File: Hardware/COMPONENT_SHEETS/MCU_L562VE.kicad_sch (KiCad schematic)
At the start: 29 parts, among them SW1 MCU Reset, U7 STM32L562VET6Q, Y3 32MHz

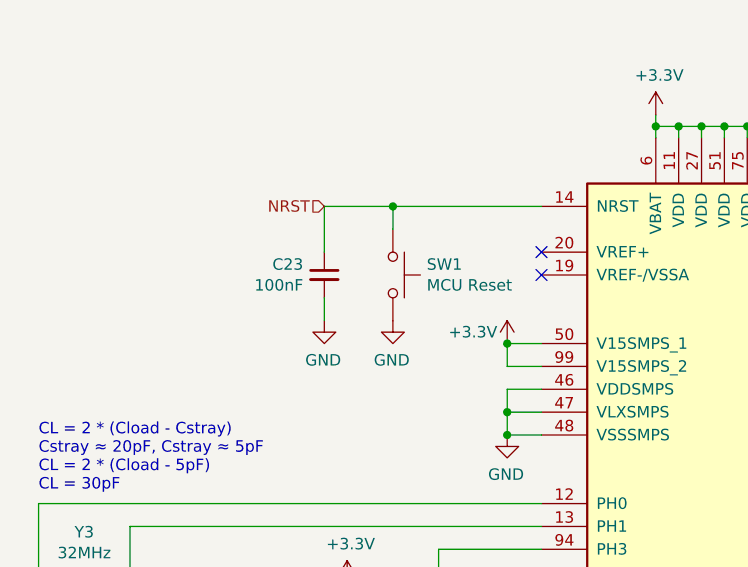
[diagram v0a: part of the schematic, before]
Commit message: Grounded VSSA
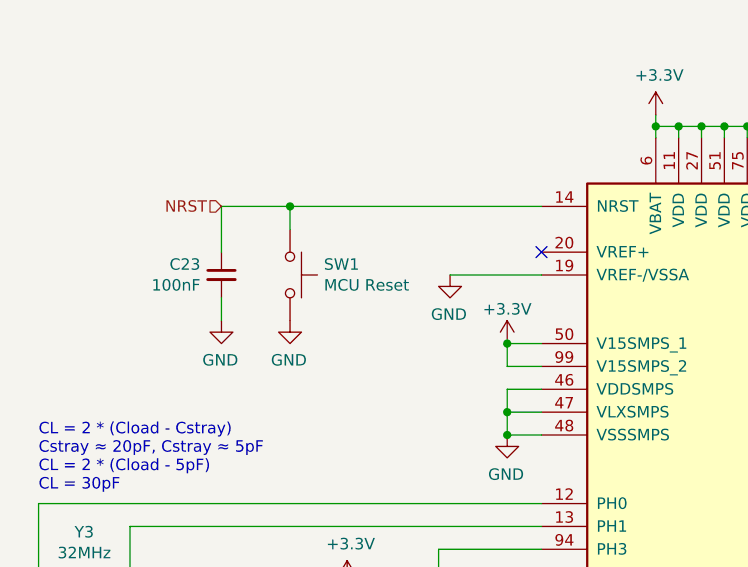
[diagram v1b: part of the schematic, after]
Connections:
- net GND: now also U7.19 (VREF-/VSSA)
- no-connect marks 48 -> 47
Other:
- moved on the sheet: C23, SW1
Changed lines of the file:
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@@
   (junction (at 100.33 173.99) (diameter 0) (color 0 0 0 0)
   )
-  (junction (at 60.96 40.64) (diameter 0) (color 0 0 0 0)
+  (junction (at 49.53 40.64) (diameter 0) (color 0 0 0 0)
   )
   (junction (at 187.96 88.9) (diameter 0) (color 0 0 0 0)
@@
   (no_connect (at 123.19 162.56))
   (no_connect (at 77.47 154.94))
-  (no_connect (at 77.47 48.26))
   (no_connect (at 123.19 101.6))
   (no_connect (at 123.19 91.44))
@@
     (stroke (width 0) (type default) (color 0 0 0 0))
   )
-  (wire (pts (xy 53.34 53.34) (xy 53.34 50.8))
-    (stroke (width 0) (type default) (color 0 0 0 0))
-  )
-  (wire (pts (xy 53.34 40.64) (xy 53.34 45.72))
+  (wire (pts (xy 41.91 53.34) (xy 41.91 50.8))
+    (stroke (width 0) (type default) (color 0 0 0 0))
+  )
+  (wire (pts (xy 41.91 40.64) (xy 41.91 45.72))
     (stroke (width 0) (type default) (color 0 0 0 0))
   )
@@
     (stroke (width 0) (type default) (color 0 0 0 0))
   )
-  (wire (pts (xy 60.96 40.64) (xy 77.47 40.64))
+  (wire (pts (xy 49.53 40.64) (xy 77.47 40.64))
     (stroke (width 0) (type default) (color 0 0 0 0))
   )
@@
     (stroke (width 0) (type default) (color 0 0 0 0))
   )
-  (wire (pts (xy 53.34 40.64) (xy 60.96 40.64))
+  (wire (pts (xy 41.91 40.64) (xy 49.53 40.64))
     (stroke (width 0) (type default) (color 0 0 0 0))
   )
@@
     (stroke (width 0) (type default) (color 0 0 0 0))
   )
+  (wire (pts (xy 77.47 48.26) (xy 67.31 48.26))
+    (stroke (width 0) (type default) (color 0 0 0 0))
+  )
   (wire (pts (xy 73.66 66.04) (xy 77.47 66.04))
     (stroke (width 0) (type default) (color 0 0 0 0))
@@
     (stroke (width 0) (type default) (color 0 0 0 0))
   )
-  (wire (pts (xy 60.96 43.18) (xy 60.96 40.64))
+  (wire (pts (xy 49.53 43.18) (xy 49.53 40.64))
     (stroke (width 0) (type default) (color 0 0 0 0))
   )
@@
     (effects (font (size 1.27 1.27)) (justify left))
   )
-  (hierarchical_label "NRST" (shape input) (at 53.34 40.64 180)
+  (hierarchical_label "NRST" (shape input) (at 41.91 40.64 180)
     (effects (font (size 1.27 1.27)) (justify right))
   )
@@
     (pin "1")
   )
-  (symbol (lib_id "Switch:SW_Push") (at 60.96 48.26 270) (unit 1)
-    (in_bom yes) (on_board yes)
-    (property "Reference" "SW1" (id 0) (at 64.7192 47.0916 90)
-      (effects (font (size 1.27 1.27)) (justify left))
-    )
-    (property "Value" "MCU Reset" (id 1) (at 64.7192 49.403 90)
-      (effects (font (size 1.27 1.27)) (justify left))
-    )
-    (property "Footprint" "Button_Switch_SMD:SW_SPST_PTS645" (id 2) (at 66.04 48.26 0)
-      (effects (font (size 1.27 1.27)) hide)
-    )
-    (property "Datasheet" "~" (id 3) (at 66.04 48.26 0)
-      (effects (font (size 1.27 1.27)) hide)
-    )
-    (property "LCSC" "C2837531 " (id 4) (at 60.96 48.26 90)
-      (effects (font (size 1.27 1.27)) hide)
-    )
-    (pin "1")
-    (pin "2")
-  )
-  (symbol (lib_id "power:GND") (at 53.34 53.34 0) (mirror y) (unit 1)
-    (in_bom yes) (on_board yes)
-    (property "Reference" "#PWR044" (id 0) (at 53.34 59.69 0)
-      (effects (font (size 1.27 1.27)) hide)
-    )
-    (property "Value" "GND" (id 1) (at 53.213 57.7342 0))
-    (property "Footprint" "" (id 2) (at 53.34 53.34 0)
-      (effects (font (size 1.27 1.27)) hide)
-    )
-    (property "Datasheet" "" (id 3) (at 53.34 53.34 0)
-      (effects (font (size 1.27 1.27)) hide)
-    )
-    (pin "1")
-  )
-  (symbol (lib_id "Device:C_Small") (at 53.34 48.26 0) (mirror y) (unit 1)
-    (in_bom yes) (on_board yes)
-    (property "Reference" "C23" (id 0) (at 51.0032 47.0916 0)
-      (effects (font (size 1.27 1.27)) (justify left))
-    )
-    (property "Value" "100nF" (id 1) (at 51.0032 49.403 0)
-      (effects (font (size 1.27 1.27)) (justify left))
-    )
-    (property "Footprint" "Capacitor_SMD:C_0603_1608Metric_Pad1.08x0.95mm_HandSolder" (id 2) (at 53.34 48.26 0)
-      (effects (font (size 1.27 1.27)) hide)
-    )
-    (property "Datasheet" "~" (id 3) (at 53.34 48.26 0)
-      (effects (font (size 1.27 1.27)) hide)
-    )
-    (property "LCSC" "C14663" (id 4) (at 53.34 48.26 0)
-      (effects (font (size 1.27 1.27)) hide)
-    )
-    (pin "1")
-    (pin "2")
-  )
-  (symbol (lib_id "power:GND") (at 60.96 53.34 0) (mirror y) (unit 1)
-    (in_bom yes) (on_board yes)
-    (property "Reference" "#PWR053" (id 0) (at 60.96 59.69 0)
-      (effects (font (size 1.27 1.27)) hide)
-    )
-    (property "Value" "GND" (id 1) (at 60.833 57.7342 0))
-    (property "Footprint" "" (id 2) (at 60.96 53.34 0)
-      (effects (font (size 1.27 1.27)) hide)
-    )
-    (property "Datasheet" "" (id 3) (at 60.96 53.34 0)
+  (symbol (lib_id "Switch:SW_Push") (at 49.53 48.26 270) (unit 1)
+    (in_bom yes) (on_board yes)
+    (property "Reference" "SW1" (id 0) (at 53.2892 47.0916 90)
+      (effects (font (size 1.27 1.27)) (justify left))
+    )
+    (property "Value" "MCU Reset" (id 1) (at 53.2892 49.403 90)
+      (effects (font (size 1.27 1.27)) (justify left))
+    )
+    (property "Footprint" "Button_Switch_SMD:SW_SPST_PTS645" (id 2) (at 54.61 48.26 0)
+      (effects (font (size 1.27 1.27)) hide)
+    )
+    (property "Datasheet" "~" (id 3) (at 54.61 48.26 0)
+      (effects (font (size 1.27 1.27)) hide)
+    )
+    (property "LCSC" "C2837531 " (id 4) (at 49.53 48.26 90)
+      (effects (font (size 1.27 1.27)) hide)
+    )
+    (pin "1")
+    (pin "2")
+  )
+  (symbol (lib_id "power:GND") (at 41.91 53.34 0) (mirror y) (unit 1)
+    (in_bom yes) (on_board yes)
+    (property "Reference" "#PWR044" (id 0) (at 41.91 59.69 0)
+      (effects (font (size 1.27 1.27)) hide)
+    )
+    (property "Value" "GND" (id 1) (at 41.783 57.7342 0))
+    (property "Footprint" "" (id 2) (at 41.91 53.34 0)
+      (effects (font (size 1.27 1.27)) hide)
+    )
+    (property "Datasheet" "" (id 3) (at 41.91 53.34 0)
+      (effects (font (size 1.27 1.27)) hide)
+    )
+    (pin "1")
+  )
+  (symbol (lib_id "Device:C_Small") (at 41.91 48.26 0) (mirror y) (unit 1)
+    (in_bom yes) (on_board yes)
+    (property "Reference" "C23" (id 0) (at 39.5732 47.0916 0)
+      (effects (font (size 1.27 1.27)) (justify left))
+    )
+    (property "Value" "100nF" (id 1) (at 39.5732 49.403 0)
+      (effects (font (size 1.27 1.27)) (justify left))
+    )
+    (property "Footprint" "Capacitor_SMD:C_0603_1608Metric_Pad1.08x0.95mm_HandSolder" (id 2) (at 41.91 48.26 0)
+      (effects (font (size 1.27 1.27)) hide)
+    )
+    (property "Datasheet" "~" (id 3) (at 41.91 48.26 0)
+      (effects (font (size 1.27 1.27)) hide)
+    )
+    (property "LCSC" "C14663" (id 4) (at 41.91 48.26 0)
+      (effects (font (size 1.27 1.27)) hide)
+    )
+    (pin "1")
+    (pin "2")
+  )
+  (symbol (lib_id "power:GND") (at 49.53 53.34 0) (mirror y) (unit 1)
+    (in_bom yes) (on_board yes)
+    (property "Reference" "#PWR053" (id 0) (at 49.53 59.69 0)
+      (effects (font (size 1.27 1.27)) hide)
+    )
+    (property "Value" "GND" (id 1) (at 49.403 57.7342 0))
+    (property "Footprint" "" (id 2) (at 49.53 53.34 0)
+      (effects (font (size 1.27 1.27)) hide)
+    )
+    (property "Datasheet" "" (id 3) (at 49.53 53.34 0)
       (effects (font (size 1.27 1.27)) hide)
     )
@@
       (effects (font (size 1.27 1.27)) hide)
     )
-    (property "Value" "+3.3V" (id 1) (at 69.85 54.61 0))
+    (property "Value" "+3.3V" (id 1) (at 73.66 52.07 0))
     (property "Footprint" "" (id 2) (at 73.66 55.88 0)
       (effects (font (size 1.27 1.27)) hide)
@@
       (effects (font (size 1.27 1.27)) hide)
     )
+    (pin "1")
+  )
+  (symbol (lib_id "power:GND") (at 67.31 48.26 0) (mirror y) (unit 1)
+    (in_bom yes) (on_board yes)
+    (property "Reference" "#PWR?" (id 0) (at 67.31 54.61 0)
+      (effects (font (size 1.27 1.27)) hide)
+    )
+    (property "Value" "GND" (id 1) (at 67.183 52.6542 0))
+    (property "Footprint" "" (id 2) (at 67.31 48.26 0)
+      (effects (font (size 1.27 1.27)) hide)
+    )
+    (property "Datasheet" "" (id 3) (at 67.31 48.26 0)
+      (effects (font (size 1.27 1.27)) hide)
+    )

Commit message: Corrected microcontroller component sheet
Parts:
- added C36, C38: 1uF, Capacitor_SMD:C_0603_1608Metric_Pad1.08x0.95mm_HandSolder, symbol Device:C_Small
- added C37: 100nF, Capacitor_SMD:C_0603_1608Metric_Pad1.08x0.95mm_HandSolder, symbol Device:C_Small
- added R11: 4.7k, Resistor_SMD:R_0603_1608Metric_Pad1.05x0.95mm_HandSolder, symbol Device:R_Small
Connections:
- net +3V3: now also U7.20 (VREF+), C36.1, C37.1, C38.1, R11.2
- net GND: now also C36.2, C37.2, C38.2
- net NRST: now also R11.1
- no-connect marks 47 -> 46
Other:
- note added: "I2C1 Pullup"
- note added: "MCU Reset"
- note removed: "I2C1 Pullup Resistors"
- moved on the sheet: C23, C24, C25, JP1, R4, R5, SW1, Y3

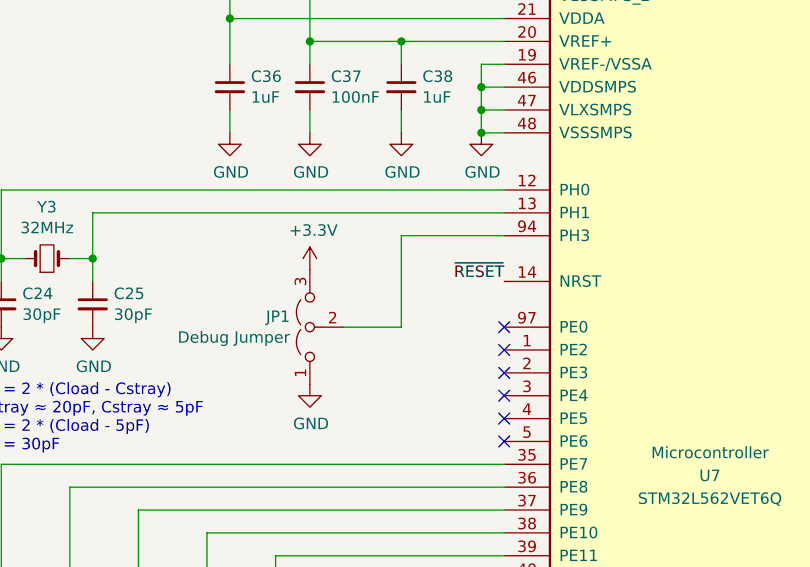
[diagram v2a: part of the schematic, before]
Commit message: Added pullup resistor for boot pin
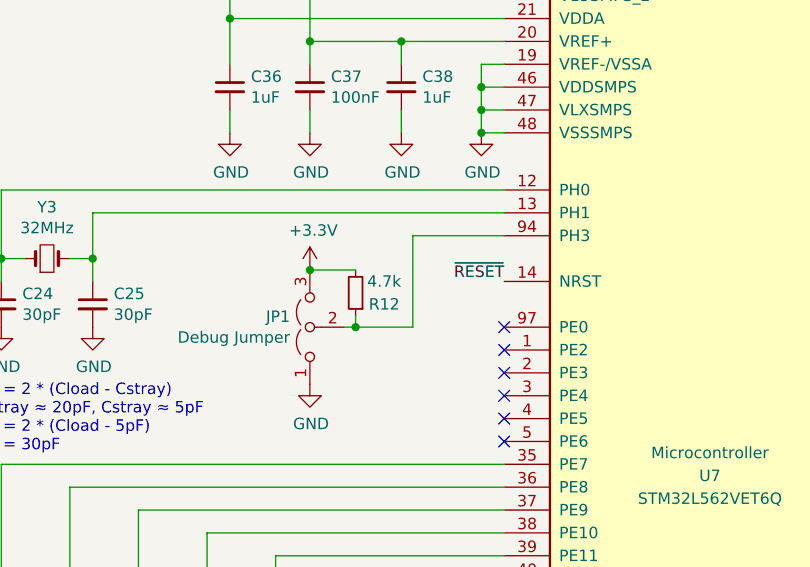
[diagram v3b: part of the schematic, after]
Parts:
- added R12: 4.7k, Resistor_SMD:R_0603_1608Metric_Pad1.05x0.95mm_HandSolder, symbol Device:R_Small
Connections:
- net +3V3: now also R12.2
- net at JP1.2 (C), U7.94 (PH3): now also R12.1
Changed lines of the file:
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@@
   (junction (at 177.8 34.29) (diameter 0) (color 0 0 0 0)
   )
+  (junction (at 55.88 80.01) (diameter 0) (color 0 0 0 0)
+  )
   (junction (at 189.23 34.29) (diameter 0) (color 0 0 0 0)
   )
@@
   )
   (junction (at 74.93 62.23) (diameter 0) (color 0 0 0 0)
+  )
+  (junction (at 60.96 86.36) (diameter 0) (color 0 0 0 0)
   )
   (junction (at 234.95 34.29) (diameter 0) (color 0 0 0 0)
@@
     (stroke (width 0) (type default) (color 0 0 0 0))
   )
+  (wire (pts (xy 55.88 80.01) (xy 60.96 80.01))
+    (stroke (width 0) (type default) (color 0 0 0 0))
+  )
   (wire (pts (xy 74.93 62.23) (xy 77.47 62.23))
     (stroke (width 0) (type default) (color 0 0 0 0))
@@
     (stroke (width 0) (type default) (color 0 0 0 0))
   )
+  (wire (pts (xy 60.96 85.09) (xy 60.96 86.36))
+    (stroke (width 0) (type default) (color 0 0 0 0))
+  )
   (wire (pts (xy 257.81 35.56) (xy 257.81 34.29))
     (stroke (width 0) (type default) (color 0 0 0 0))
@@
     (stroke (width 0) (type default) (color 0 0 0 0))
   )
-  (wire (pts (xy 59.69 86.36) (xy 66.04 86.36))
+  (wire (pts (xy 59.69 86.36) (xy 60.96 86.36))
     (stroke (width 0) (type default) (color 0 0 0 0))
   )
@@
     (stroke (width 0) (type default) (color 0 0 0 0))
   )
+  (wire (pts (xy 60.96 86.36) (xy 67.31 86.36))
+    (stroke (width 0) (type default) (color 0 0 0 0))
+  )
   (wire (pts (xy 95.25 31.75) (xy 97.79 31.75))
     (stroke (width 0) (type default) (color 0 0 0 0))
@@
     (stroke (width 0) (type default) (color 0 0 0 0))
   )
-  (wire (pts (xy 66.04 76.2) (xy 77.47 76.2))
+  (wire (pts (xy 67.31 76.2) (xy 77.47 76.2))
     (stroke (width 0) (type default) (color 0 0 0 0))
   )
@@
     (stroke (width 0) (type default) (color 0 0 0 0))
   )
-  (wire (pts (xy 66.04 86.36) (xy 66.04 76.2))
+  (wire (pts (xy 67.31 86.36) (xy 67.31 76.2))
     (stroke (width 0) (type default) (color 0 0 0 0))
   )
@@
     (pin "1")
   )
+  (symbol (lib_id "Device:R_Small") (at 60.96 82.55 180) (unit 1)
+    (in_bom yes) (on_board yes)
+    (property "Reference" "R12" (id 0) (at 64.135 83.82 0))
+    (property "Value" "4.7k" (id 1) (at 64.135 81.28 0))
+    (property "Footprint" "Resistor_SMD:R_0603_1608Metric_Pad1.05x0.95mm_HandSolder" (id 2) (at 60.96 82.55 0)
+      (effects (font (size 1.27 1.27)) hide)
+    )
+    (property "Datasheet" "~" (id 3) (at 60.96 82.55 0)
+      (effects (font (size 1.27 1.27)) hide)
+    )
+    (property "LCSC" " C23253 " (id 4) (at 60.96 82.55 0)
+      (effects (font (size 1.27 1.27)) hide)
+    )
+    (pin "1")
+    (pin "2")
+  )
   (symbol (lib_id "power:+3.3V") (at 55.88 49.53 0) (unit 1)

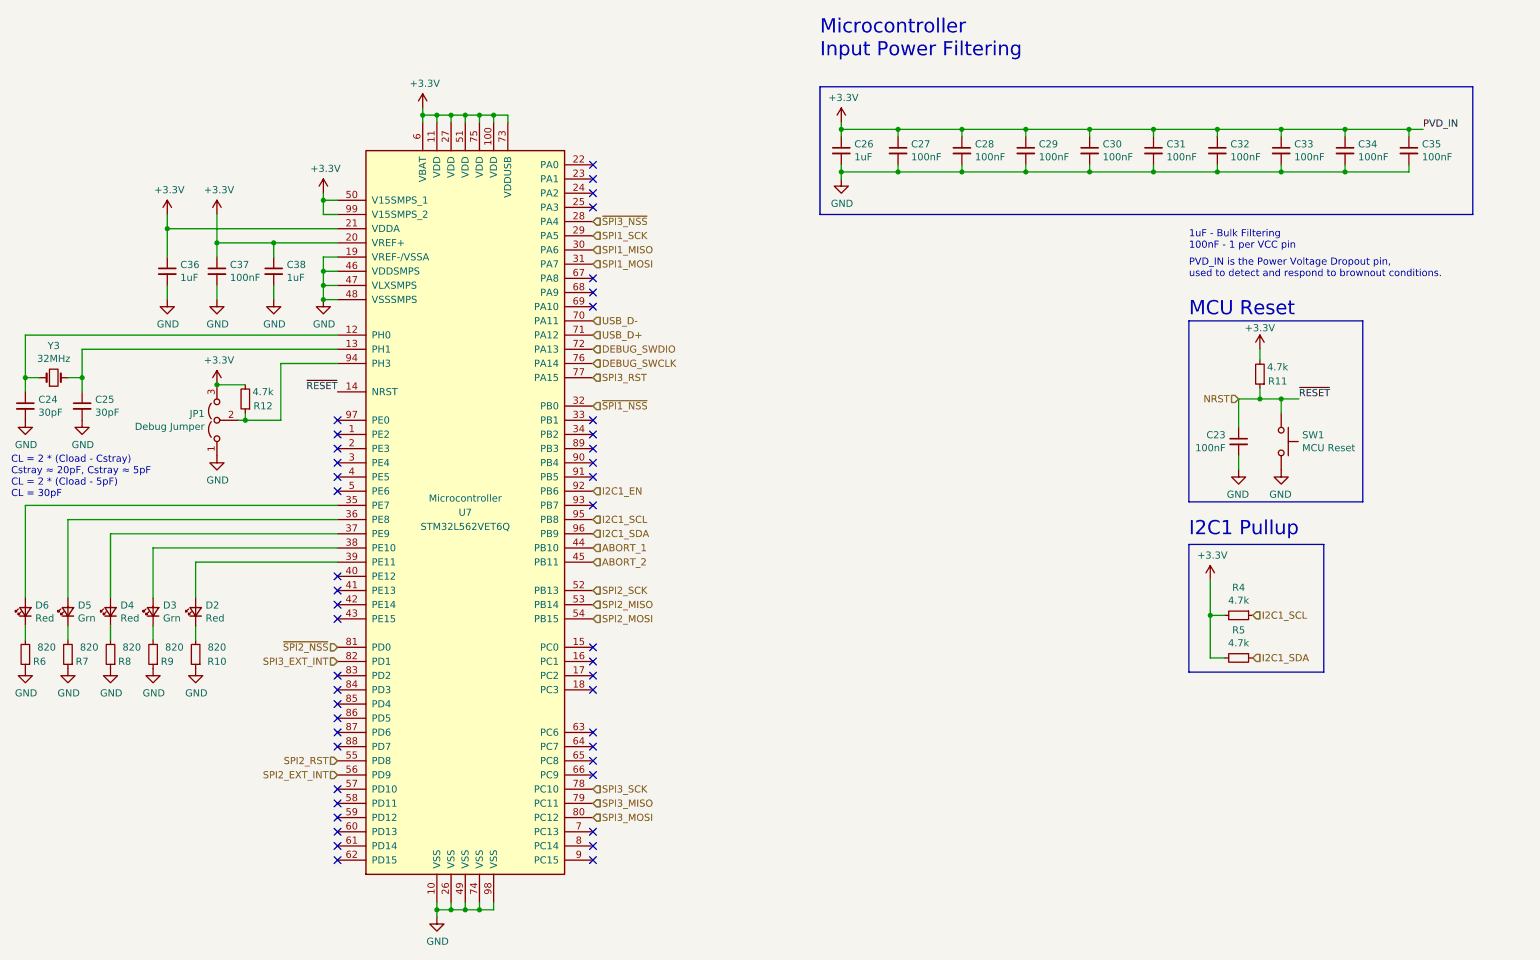
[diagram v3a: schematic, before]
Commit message: Increased spacing around MCU, added filter caps for SMPS, rerouted 5V from DSUB, changed SMA to right angle
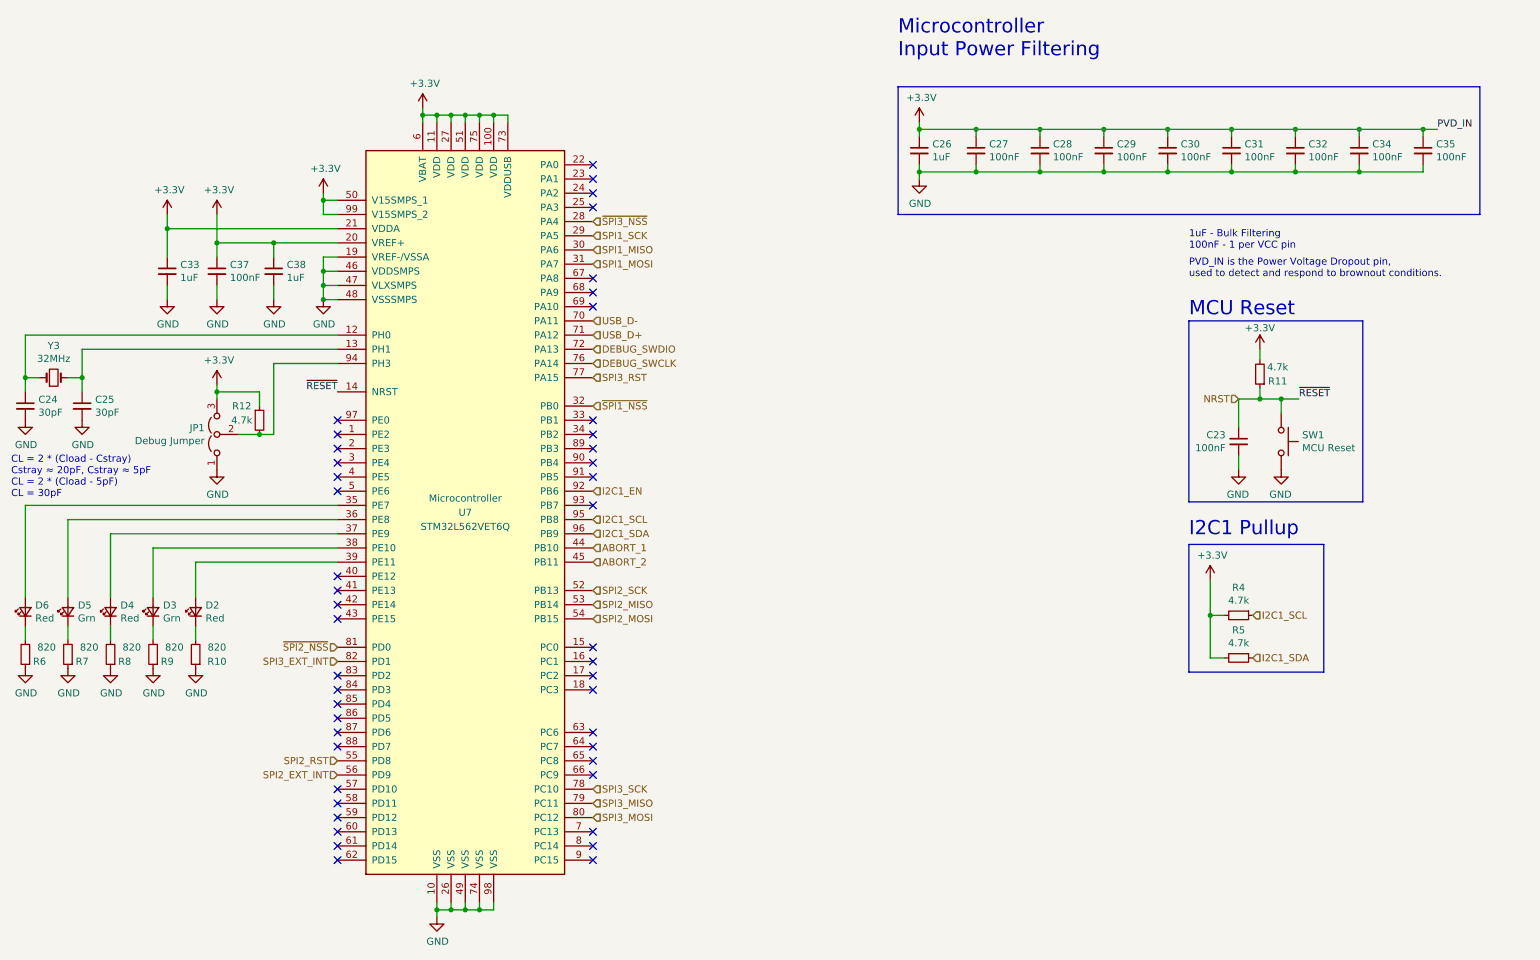
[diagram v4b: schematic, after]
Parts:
- removed C33: 100nF, Capacitor_SMD:C_0603_1608Metric_Pad1.08x0.95mm_HandSolder, symbol Device:C_Small
- R12: footprint Resistor_SMD:R_0603_1608Metric_Pad1.05x0.95mm_HandSolder -> Resistor_SMD:R_0201_0603Metric_Pad0.64x0.40mm_HandSolder; LCSC C23253 -> C25999
- renumbered C36 to C33
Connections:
- net +3V3: now also R12.1; no longer R12.2
- net at JP1.2 (C), U7.94 (PH3): now also R12.2; no longer R12.1
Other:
- moved on the sheet: C26, C27, C28, C29, C30, C31, C32, C34, C35, JP1

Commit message: Updated schematic labels, Version 2.0.0
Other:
- company: (none) -> When HAMs Fly Senior Design Team
- title: (none) -> Main Control Chip
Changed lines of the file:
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@@
 (kicad_sch (version 20211123) (generator eeschema)
   (paper "A4")
+  (title_block
+    (title "Main Control Chip")
+    (date "2022-03-24")
+    (rev "v2.0.0")
+    (company "When HAMs Fly Senior Design Team")
+    (comment 1 "https://github.com/MSTRocketDesignTeam/Avionics-Telemetry-PCB")
+    (comment 2 "Board Revision 2")
+    (comment 3 "Schematic depicting logical connections between components")
+  )
   (junction (at 74.93 46.99) (diameter 0) (color 0 0 0 0)
   )
